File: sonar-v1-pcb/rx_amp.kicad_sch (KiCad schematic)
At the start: 13 parts, among them U2 Opamp_Dual

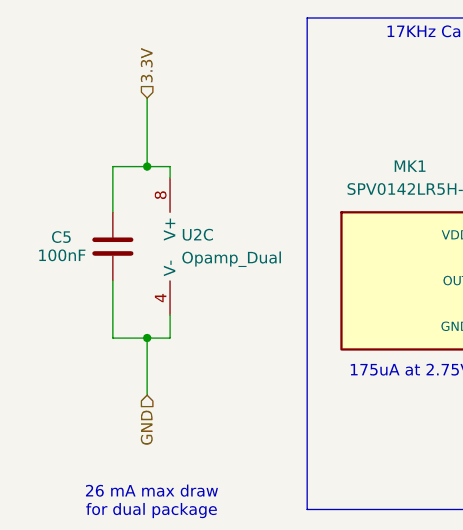
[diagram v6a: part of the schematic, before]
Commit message: Fix some stuff kinda in the short term but this should be fixed long term
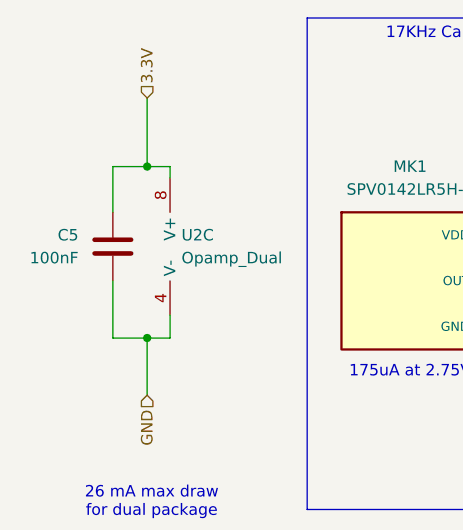
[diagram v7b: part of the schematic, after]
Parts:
- removed C5: 100nF, Capacitor_SMD:C_0402_1005Metric, symbol Device:C
- added C5: 100nF, GS_Capacitors:C_0603_1608Metric, symbol GS_Capacitor_0603:C_0603_100nF
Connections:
- net 3.3V: now also C5.1
- net GND: now also C5.2
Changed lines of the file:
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@@
 	)
 	(symbol
-		(lib_id "Device:C")
+		(lib_id "GS_Capacitor_0603:C_0603_100nF")
 		(at 29.21 50.8 0)
 		(unit 1)
@@
 		(dnp no)
 		(property "Reference" "C5"
-			(at 22.352 49.784 0)
+			(at 25.4 49.5299 0)
 			(show_name no)
 			(do_not_autoplace no)
@@
 					(size 1.27 1.27)
 				)
-				(justify left)
+				(justify right)
 			)
 		)
 		(property "Value" "100nF"
-			(at 20.828 51.816 0)
+			(at 25.4 52.0699 0)
 			(show_name no)
 			(do_not_autoplace no)
@@
 					(size 1.27 1.27)
 				)
-				(justify left)
+				(justify right)
 			)
 		)
-		(property "Footprint" "Capacitor_SMD:C_0402_1005Metric"
-			(at 30.1752 54.61 0)
+		(property "Footprint" "GS_Capacitors:C_0603_1608Metric"
+			(at 29.21 28.448 0)
 			(hide yes)
 			(show_name no)
@@
 			)
 		)
-		(property "Datasheet" ""
-			(at 29.21 50.8 0)
+		(property "Datasheet" "https://www.lcsc.com/datasheet/C14663.pdf"
+			(at 29.21 37.084 0)
 			(hide yes)
 			(show_name no)
@@
 			)
 		)
-		(property "Description" "Unpolarized capacitor"
-			(at 29.21 50.8 0)
+		(property "Description" "100nF 10% Unpolarized Capacitor, 50V Max Voltage, X7R"
+			(at 29.21 35.052 0)
 			(hide yes)
 			(show_name no)
@@
 			)
 		)
-		(pin "1"
+		(property "Manufacturer" "YAGEO"
+			(at 29.21 31.75 0)
+			(hide yes)
+			(show_name no)
+			(do_not_autoplace no)
+			(effects
+				(font
+					(size 1.27 1.27)
+				)
+			)
+		)
+		(property "MPN" "CC0603KRX7R9BB104"
+			(at 29.21 33.528 0)
+			(hide yes)
+			(show_name no)
+			(do_not_autoplace no)
+			(effects
+				(font
+					(size 1.27 1.27)
+				)
+			)
+		)
+		(property "LCSC ID" "C14663"
+			(at 29.21 38.862 0)
+			(hide yes)
+			(show_name no)
+			(do_not_autoplace no)
+			(effects
+				(font
+					(size 1.27 1.27)
+				)
+			)
+		)
+		(property "Package" "0603"
+			(at 29.21 30.226 0)
+			(hide yes)
+			(show_name no)
+			(do_not_autoplace no)
+			(effects
+				(font
+					(size 1.27 1.27)
+				)
+			)
 		)
 		(pin "2"
+		)
+		(pin "1"
 		)
 		(instances
@@
 					(unit 1)
 				)
-			)
-			(project "sonar"
-				(path "/f72ceae0-eee4-4385-b0e8-639846bcb5f2/293969c4-9575-41aa-bb6a-e94ffb52e407/1e9737bb-54d3-46c6-89c7-bafd5d01cb9f"
-					(reference "C2702")
-					(unit 1)
-				)
-				(path "/f72ceae0-eee4-4385-b0e8-639846bcb5f2/293969c4-9575-41aa-bb6a-e94ffb52e407/4b88e5a9-a1a4-4236-ac8a-a515268f9e7e"
-					(reference "C2402")
-					(unit 1)
-				)
-				(path "/f72ceae0-eee4-4385-b0e8-639846bcb5f2/293969c4-9575-41aa-bb6a-e94ffb52e407/4baae0c7-5504-4fa5-b170-826798e08abe"
-					(reference "C2102")
-					(unit 1)
-				)
-				(path "/f72ceae0-eee4-4385-b0e8-639846bcb5f2/293969c4-9575-41aa-bb6a-e94ffb52e407/5fa345fd-8f82-4102-b4da-88393397ee2f"
-					(reference "C2502")
-					(unit 1)
-				)
-				(path "/f72ceae0-eee4-4385-b0e8-639846bcb5f2/293969c4-9575-41aa-bb6a-e94ffb52e407/92589eb0-14ab-438f-abf4-d7e391dbea95"
-					(reference "C2002")
-					(unit 1)
-				)
-				(path "/f72ceae0-eee4-4385-b0e8-639846bcb5f2/293969c4-9575-41aa-bb6a-e94ffb52e407/a69a1e19-7333-49c9-8cfe-abe95e31b9e6"
-					(reference "C1902")
-					(unit 1)
-				)
-				(path "/f72ceae0-eee4-4385-b0e8-639846bcb5f2/293969c4-9575-41aa-bb6a-e94ffb52e407/da58af52-59a2-42c6-b6e7-fabe3f18277b"
-					(reference "C2302")
-					(unit 1)
-				)
-				(path "/f72ceae0-eee4-4385-b0e8-639846bcb5f2/293969c4-9575-41aa-bb6a-e94ffb52e407/ef24f3d1-799c-40c0-a32b-fd2185333268"
-					(reference "C2802")
-					(unit 1)
-				)
-				(path "/f72ceae0-eee4-4385-b0e8-639846bcb5f2/d3b8d639-c387-46bd-9010-317ff5495a13/1e9737bb-54d3-46c6-89c7-bafd5d01cb9f"
-					(reference "C1502")
-					(unit 1)
-				)
-				(path "/f72ceae0-eee4-4385-b0e8-639846bcb5f2/d3b8d639-c387-46bd-9010-317ff5495a13/4b88e5a9-a1a4-4236-ac8a-a515268f9e7e"
-					(reference "C1202")
-					(unit 1)
-				)
-				(path "/f72ceae0-eee4-4385-b0e8-639846bcb5f2/d3b8d639-c387-46bd-9010-317ff5495a13/4baae0c7-5504-4fa5-b170-826798e08abe"
-					(reference "C902")
-					(unit 1)
-				)
-				(path "/f72ceae0-eee4-4385-b0e8-639846bcb5f2/d3b8d639-c387-46bd-9010-317ff5495a13/5fa345fd-8f82-4102-b4da-88393397ee2f"
-					(reference "C1302")
-					(unit 1)
-				)
-				(path "/f72ceae0-eee4-4385-b0e8-639846bcb5f2/d3b8d639-c387-46bd-9010-317ff5495a13/92589eb0-14ab-438f-abf4-d7e391dbea95"
-					(reference "C802")
-					(unit 1)
-				)
-				(path "/f72ceae0-eee4-4385-b0e8-639846bcb5f2/d3b8d639-c387-46bd-9010-317ff5495a13/a69a1e19-7333-49c9-8cfe-abe95e31b9e6"
-					(reference "C502")
-					(unit 1)
-				)
-				(path "/f72ceae0-eee4-4385-b0e8-639846bcb5f2/d3b8d639-c387-46bd-9010-317ff5495a13/da58af52-59a2-42c6-b6e7-fabe3f18277b"
-					(reference "C1102")
-					(unit 1)
-				)
-				(path "/f72ceae0-eee4-4385-b0e8-639846bcb5f2/d3b8d639-c387-46bd-9010-317ff5495a13/ef24f3d1-799c-40c0-a32b-fd2185333268"
-					(reference "C1602")
-					(unit 1)
-				)
-				(path "/f72ceae0-eee4-4385-b0e8-639846bcb5f2/d78844ef-eb5d-4b24-a5c3-8824db20c2bc/1e9737bb-54d3-46c6-89c7-bafd5d01cb9f"
-					(reference "C2602")
-					(unit 1)
-				)
-				(path "/f72ceae0-eee4-4385-b0e8-639846bcb5f2/d78844ef-eb5d-4b24-a5c3-8824db20c2bc/4b88e5a9-a1a4-4236-ac8a-a515268f9e7e"
-					(reference "C702")
-					(unit 1)
-				)
-				(path "/f72ceae0-eee4-4385-b0e8-639846bcb5f2/d78844ef-eb5d-4b24-a5c3-8824db20c2bc/4baae0c7-5504-4fa5-b170-826798e08abe"
-					(reference "C302")
-					(unit 1)
-				)
-				(path "/f72ceae0-eee4-4385-b0e8-639846bcb5f2/d78844ef-eb5d-4b24-a5c3-8824db20c2bc/5fa345fd-8f82-4102-b4da-88393397ee2f"
-					(reference "C1802")
-					(unit 1)
-				)
-				(path "/f72ceae0-eee4-4385-b0e8-639846bcb5f2/d78844ef-eb5d-4b24-a5c3-8824db20c2bc/92589eb0-14ab-438f-abf4-d7e391dbea95"
-					(reference "C602")
-					(unit 1)
-				)
-				(path "/f72ceae0-eee4-4385-b0e8-639846bcb5f2/d78844ef-eb5d-4b24-a5c3-8824db20c2bc/a69a1e19-7333-49c9-8cfe-abe95e31b9e6"
-					(reference "C1402")
-					(unit 1)
-				)
-				(path "/f72ceae0-eee4-4385-b0e8-639846bcb5f2/d78844ef-eb5d-4b24-a5c3-8824db20c2bc/da58af52-59a2-42c6-b6e7-fabe3f18277b"
-					(reference "C1002")
-					(unit 1)
-				)
-				(path "/f72ceae0-eee4-4385-b0e8-639846bcb5f2/d78844ef-eb5d-4b24-a5c3-8824db20c2bc/ef24f3d1-799c-40c0-a32b-fd2185333268"
-					(reference "C2202")
-					(unit 1)
-				)

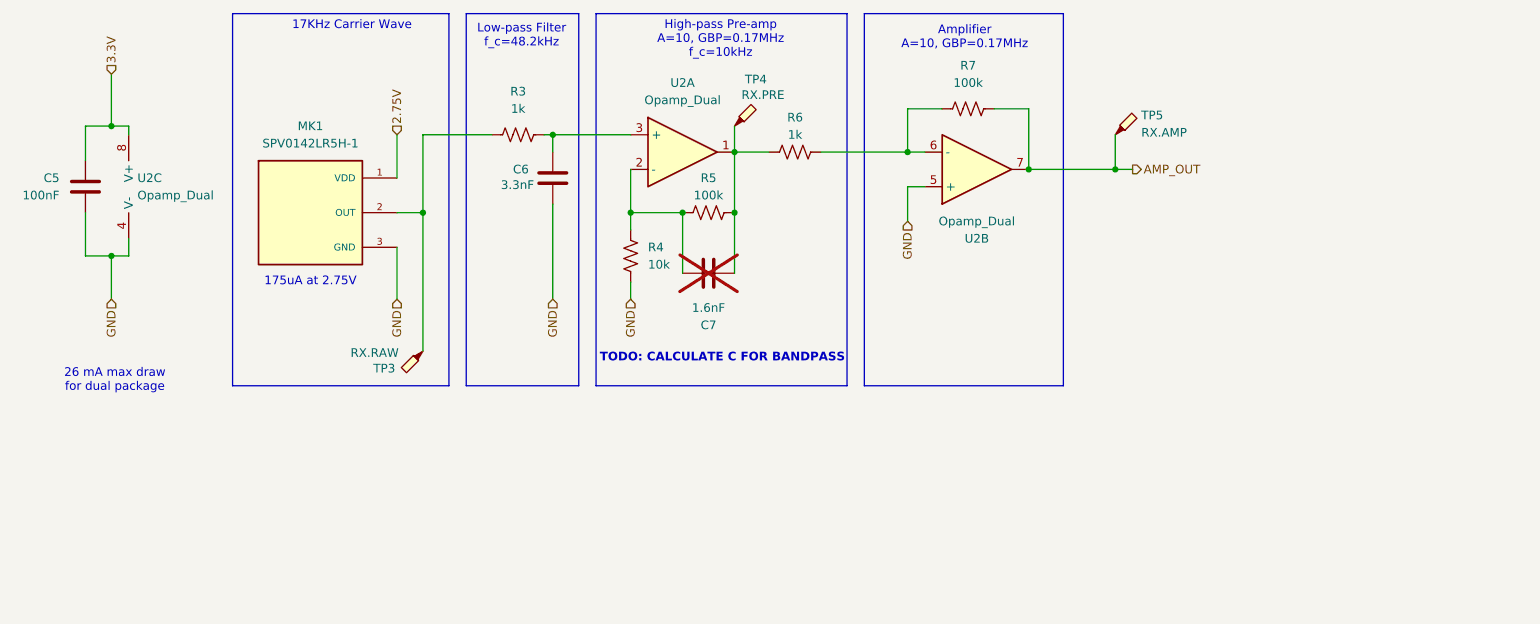
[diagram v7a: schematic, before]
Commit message: Add an h-bridge
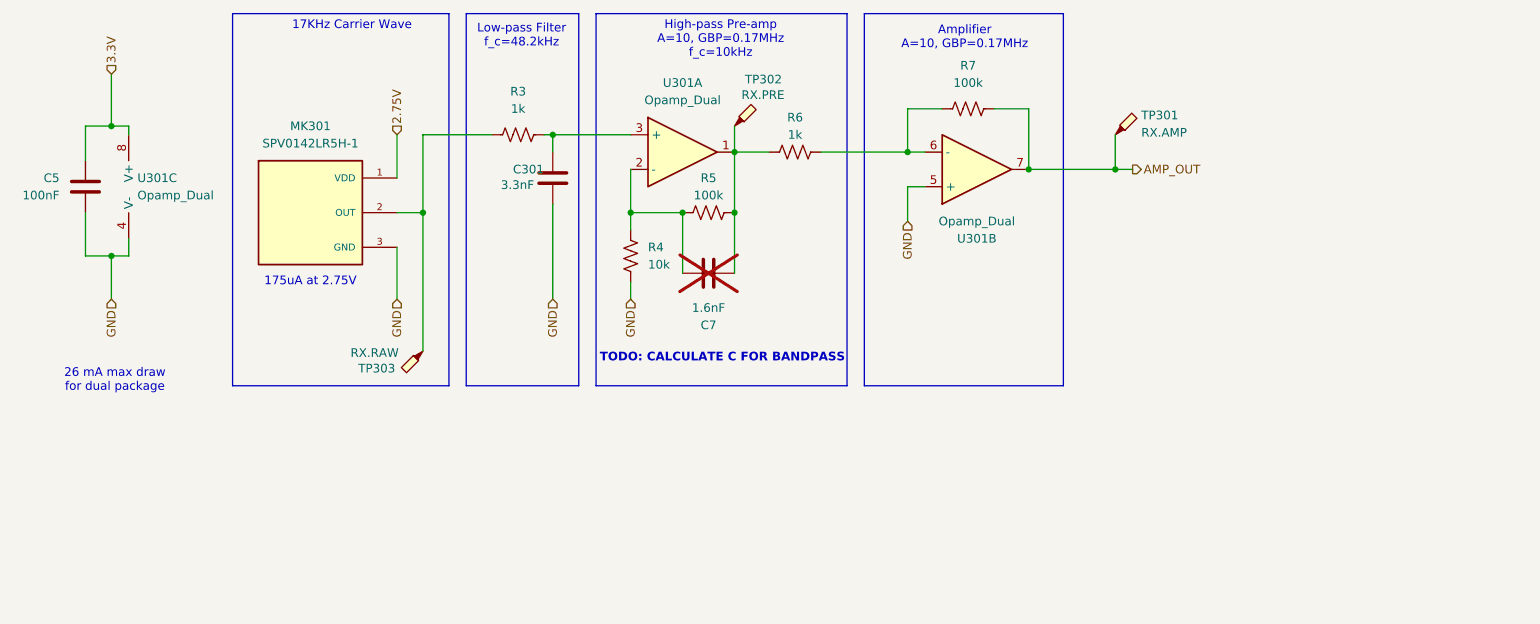
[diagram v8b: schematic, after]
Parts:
- renumbered C6 to C301, MK1 to MK301, TP5 to TP301, TP4 to TP302, TP3 to TP303, U2 to U301
